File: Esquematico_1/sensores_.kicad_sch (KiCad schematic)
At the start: 12 parts, among them U1 ICM-42688-P, U3 Mag, U4 BMP388

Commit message: Footprints
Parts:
- R1, R2: footprint (none) -> Resistor_SMD:R_0805_2012Metric_Pad1.20x1.40mm_HandSolder
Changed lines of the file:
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@@
 			)
 		)
-		(property "Footprint" ""
+		(property "Footprint" "Resistor_SMD:R_0805_2012Metric_Pad1.20x1.40mm_HandSolder"
 			(at 27.432 78.74 90)
 			(effects
@@
 			)
 		)
-		(property "Footprint" ""
+		(property "Footprint" "Resistor_SMD:R_0805_2012Metric_Pad1.20x1.40mm_HandSolder"
 			(at 52.832 78.74 90)
 			(effects

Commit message: LDS y gran corrección de errores del esquemático
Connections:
- net GND: now also C1.2, U4.8 (VSS__1), U4.9 (VSS__2)
- no-connect marks 3 -> 13
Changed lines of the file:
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@@
 	(text_box "Especificaciones:\nSCK:\nSDA:\nVDD:\nGND:\nC1:\nGND:\nNC:\n"
 		(exclude_from_sim no)
-		(at 13.97 114.3 0)
-		(size 66.04 30.48)
+		(at 13.97 113.03 0)
+		(size 66.04 20.32)
 		(margins 0.9525 0.9525 0.9525 0.9525)
 		(stroke
@@
 	)
 	(junction
-		(at 158.75 104.14)
-		(diameter 0)
-		(color 0 0 0 0)
-	)
-	(junction
 		(at 86.36 49.53)
 		(diameter 0)
@@
 	)
 	(junction
+		(at 154.94 104.14)
+		(diameter 0)
+		(color 0 0 0 0)
+	)
+	(junction
 		(at 110.49 26.67)
 		(diameter 0)
@@
 	)
 	(junction
+		(at 143.51 104.14)
+		(diameter 0)
+		(color 0 0 0 0)
+	)
+	(junction
 		(at 99.06 29.21)
 		(diameter 0)
@@
 	)
 	(junction
-		(at 154.94 101.6)
+		(at 154.94 107.95)
 		(diameter 0)
 		(color 0 0 0 0)
@@
 	)
 	(no_connect
+		(at 35.56 93.98)
+	)
+	(no_connect
 		(at 83.82 39.37)
 	)
 	(no_connect
+		(at 35.56 101.6)
+	)
+	(no_connect
+		(at 35.56 88.9)
+	)
+	(no_connect
 		(at 83.82 44.45)
 	)
 	(no_connect
+		(at 53.34 93.98)
+	)
+	(no_connect
+		(at 53.34 88.9)
+	)
+	(no_connect
+		(at 35.56 91.44)
+	)
+	(no_connect
 		(at 83.82 41.91)
 	)
+	(no_connect
+		(at 53.34 86.36)
+	)
+	(no_connect
+		(at 35.56 99.06)
+	)
+	(no_connect
+		(at 53.34 91.44)
+	)
+	(no_connect
+		(at 35.56 96.52)
+	)
 	(wire
 		(pts
@@
 	(wire
 		(pts
+			(xy 140.97 106.68) (xy 143.51 106.68)
+		)
+		(stroke
+			(width 0)
+			(type default)
+		)
+	)
+	(wire
+		(pts
+			(xy 158.75 107.95) (xy 154.94 107.95)
+		)
+		(stroke
+			(width 0)
+			(type default)
+		)
+	)
+	(wire
+		(pts
 			(xy 26.67 83.82) (xy 29.21 83.82)
 		)
@@
 	(wire
 		(pts
+			(xy 143.51 101.6) (xy 143.51 104.14)
+		)
+		(stroke
+			(width 0)
+			(type default)
+		)
+	)
+	(wire
+		(pts
 			(xy 140.97 78.74) (xy 158.75 78.74)
 		)
@@
 	(wire
 		(pts
-			(xy 154.94 96.52) (xy 154.94 101.6)
-		)
-		(stroke
-			(width 0)
-			(type default)
-		)
-	)
-	(wire
-		(pts
 			(xy 154.94 74.93) (xy 158.75 74.93)
 		)
@@
 	(wire
 		(pts
+			(xy 154.94 104.14) (xy 154.94 107.95)
+		)
+		(stroke
+			(width 0)
+			(type default)
+		)
+	)
+	(wire
+		(pts
 			(xy 110.49 26.67) (xy 121.92 26.67)
 		)
@@
 	(wire
 		(pts
+			(xy 143.51 104.14) (xy 154.94 104.14)
+		)
+		(stroke
+			(width 0)
+			(type default)
+		)
+	)
+	(wire
+		(pts
 			(xy 27.94 39.37) (xy 33.02 39.37)
 		)
@@
 	(wire
 		(pts
+			(xy 143.51 106.68) (xy 143.51 104.14)
+		)
+		(stroke
+			(width 0)
+			(type default)
+		)
+	)
+	(wire
+		(pts
 			(xy 83.82 34.29) (xy 85.09 34.29)
 		)
@@
 	(wire
 		(pts
-			(xy 140.97 106.68) (xy 158.75 106.68)
-		)
-		(stroke
-			(width 0)
-			(type default)
-		)
-	)
-	(wire
-		(pts
 			(xy 53.34 96.52) (xy 57.15 96.52)
 		)
@@
 	(wire
 		(pts
-			(xy 140.97 101.6) (xy 154.94 101.6)
-		)
-		(stroke
-			(width 0)
-			(type default)
-		)
-	)
-	(wire
-		(pts
 			(xy 29.21 82.55) (xy 29.21 83.82)
 		)
@@
 	(wire
 		(pts
+			(xy 154.94 107.95) (xy 154.94 109.22)
+		)
+		(stroke
+			(width 0)
+			(type default)
+		)
+	)
+	(wire
+		(pts
 			(xy 27.94 44.45) (xy 33.02 44.45)
 		)
@@
 	(wire
 		(pts
-			(xy 158.75 104.14) (xy 158.75 90.17)
+			(xy 158.75 90.17) (xy 158.75 107.95)
 		)
 		(stroke
@@
 	(wire
 		(pts
+			(xy 140.97 101.6) (xy 143.51 101.6)
+		)
+		(stroke
+			(width 0)
+			(type default)
+		)
+	)
+	(wire
+		(pts
 			(xy 121.92 26.67) (xy 121.92 25.4)
 		)
@@
 	(wire
 		(pts
-			(xy 140.97 104.14) (xy 158.75 104.14)
-		)
-		(stroke
-			(width 0)
-			(type default)
-		)
-	)
-	(wire
-		(pts
-			(xy 158.75 106.68) (xy 158.75 104.14)
-		)
-		(stroke
-			(width 0)
-			(type default)
-		)
-	)
-	(wire
-		(pts
 			(xy 58.42 99.06) (xy 58.42 96.52)
 		)
@@
 	(wire
 		(pts
+			(xy 140.97 104.14) (xy 143.51 104.14)
+		)
+		(stroke
+			(width 0)
+			(type default)
+		)
+	)
+	(wire
+		(pts
 			(xy 54.61 72.39) (xy 29.21 72.39)
 		)
@@
 	(wire
 		(pts
-			(xy 154.94 101.6) (xy 154.94 109.22)
-		)
-		(stroke
+			(xy 154.94 96.52) (xy 154.94 104.14)
+		)
+		(stroke

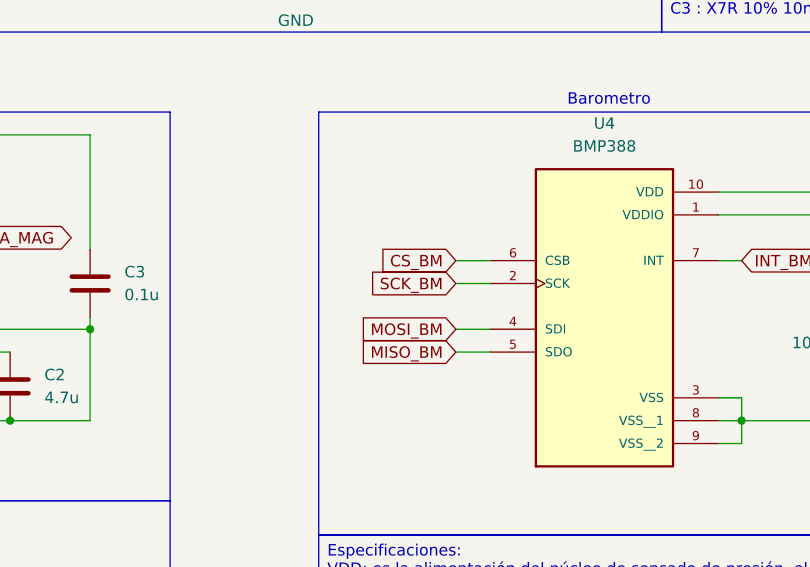
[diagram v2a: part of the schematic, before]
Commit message: Cambios netclasses, rules en el PCB, conección de los cristales
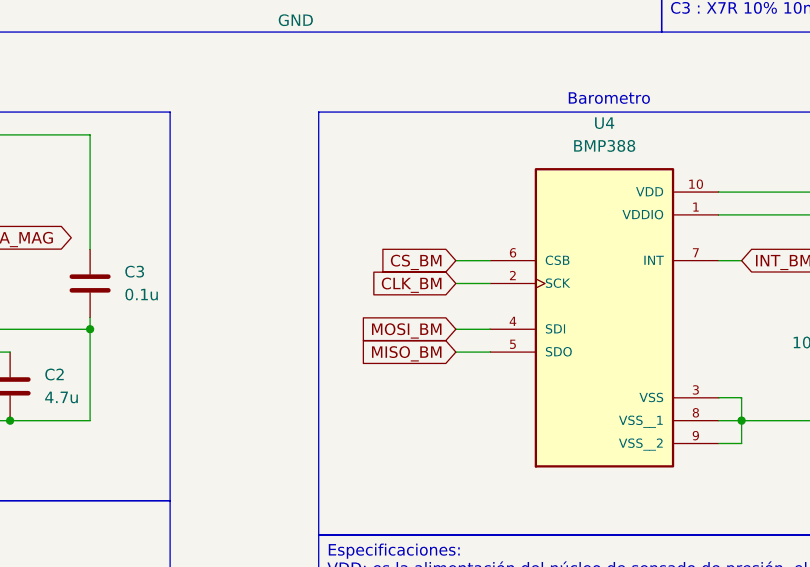
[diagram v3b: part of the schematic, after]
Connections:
- net SCK_BM renamed CLK_BM
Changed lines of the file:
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@@
 		)
 	)
-	(global_label "SCK_BM"
+	(global_label "CLK_BM"
 		(shape input)
 		(at 111.76 88.9 180)
@@
 		)
 		(property "Intersheetrefs" "${INTERSHEET_REFS}"
-			(at 101.3363 88.9 0)
+			(at 101.5177 88.9 0)
 			(effects
 				(font

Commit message: Cristal corregido
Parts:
- C1, C4: footprint Capacitor_SMD:C_0805_2012Metric_Pad1.18x1.45mm_HandSolder -> Capacitor_SMD:C_0603_1608Metric_Pad1.08x0.95mm_HandSolder
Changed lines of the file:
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@@
 			)
 		)
-		(property "Footprint" "Capacitor_SMD:C_0805_2012Metric_Pad1.18x1.45mm_HandSolder"
+		(property "Footprint" "Capacitor_SMD:C_0603_1608Metric_Pad1.08x0.95mm_HandSolder"
 			(at 159.7152 90.17 0)
 			(effects
@@
 			)
 		)
-		(property "Footprint" "Capacitor_SMD:C_0805_2012Metric_Pad1.18x1.45mm_HandSolder"
+		(property "Footprint" "Capacitor_SMD:C_0603_1608Metric_Pad1.08x0.95mm_HandSolder"
 			(at 155.9052 96.52 0)
 			(effects

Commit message: Cambio de la SD, re ruteo del ESC para mayor fiabilidad, correción en el clearence
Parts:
- C11, C9: footprint Capacitor_SMD:C_0805_2012Metric_Pad1.18x1.45mm_HandSolder -> Capacitor_SMD:C_0603_1608Metric_Pad1.08x0.95mm_HandSolder
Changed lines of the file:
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@@
 			)
 		)
-		(property "Footprint" "Capacitor_SMD:C_0805_2012Metric_Pad1.18x1.45mm_HandSolder"
+		(property "Footprint" "Capacitor_SMD:C_0603_1608Metric_Pad1.08x0.95mm_HandSolder"
 			(at 111.4552 36.83 0)
 			(effects
@@
 			)
 		)
-		(property "Footprint" "Capacitor_SMD:C_0805_2012Metric_Pad1.18x1.45mm_HandSolder"
+		(property "Footprint" "Capacitor_SMD:C_0603_1608Metric_Pad1.08x0.95mm_HandSolder"
 			(at 100.0252 38.1 0)
 			(effects

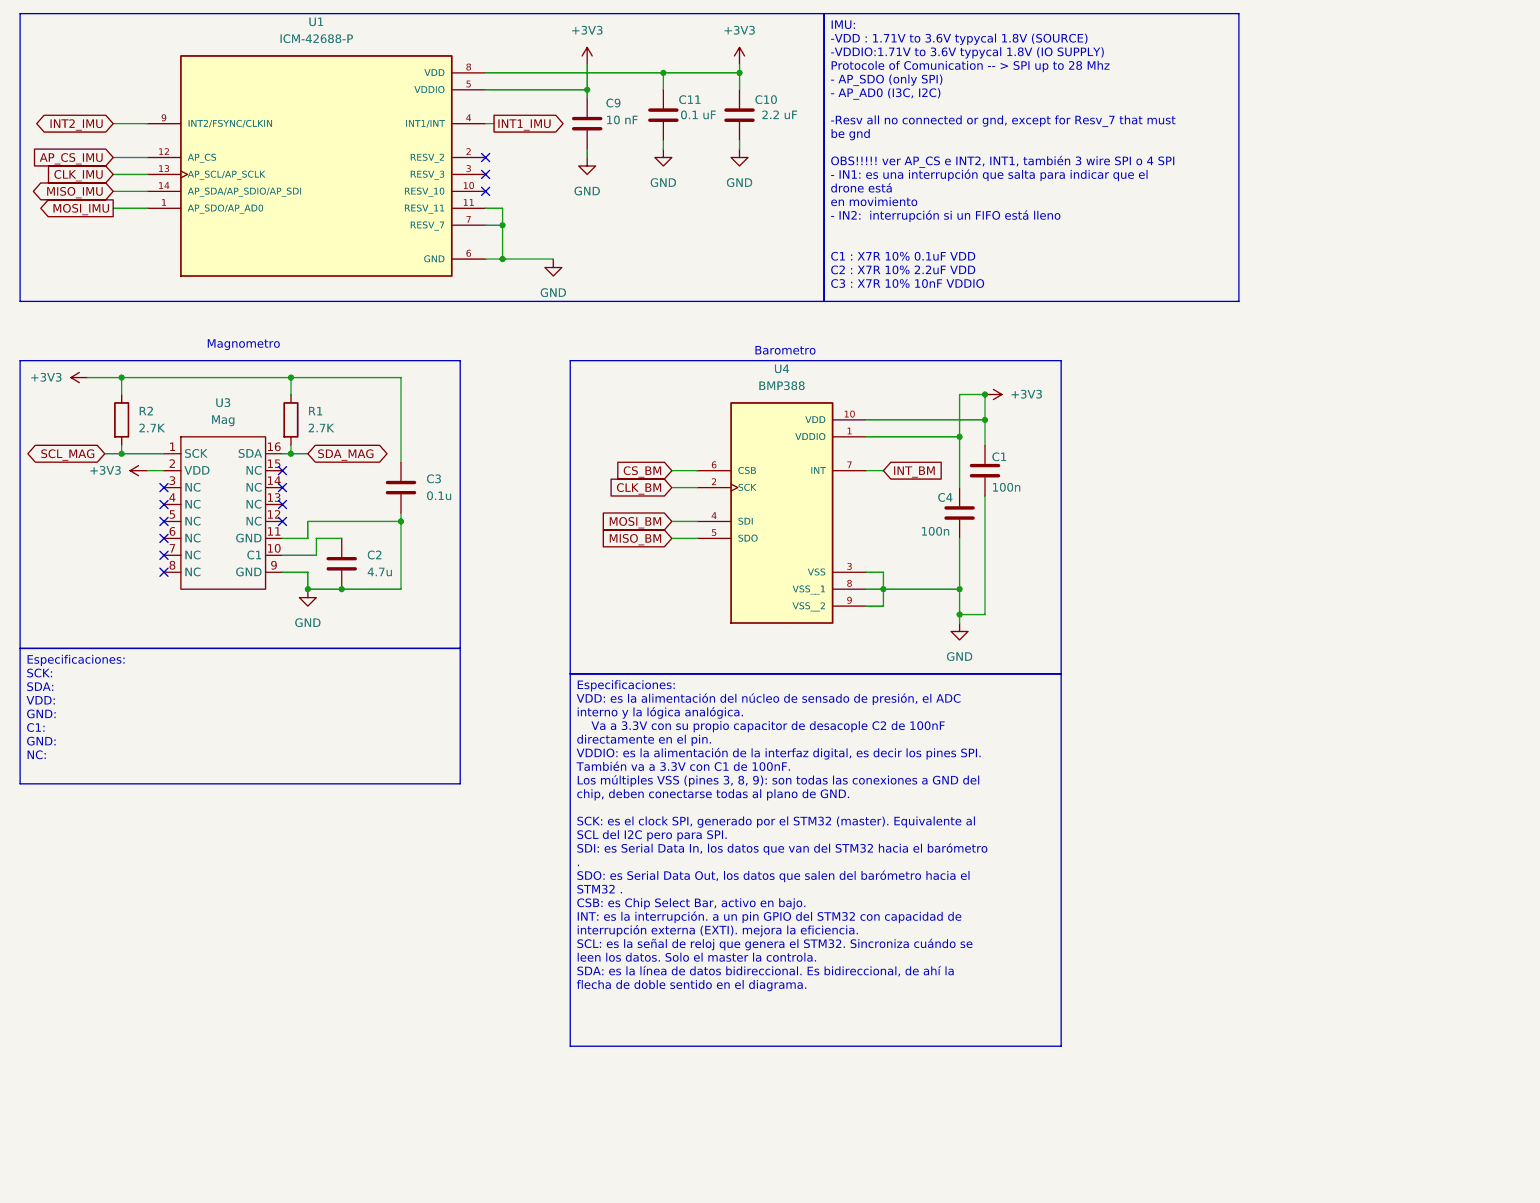
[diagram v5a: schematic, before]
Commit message: Cambio de magnometro :c
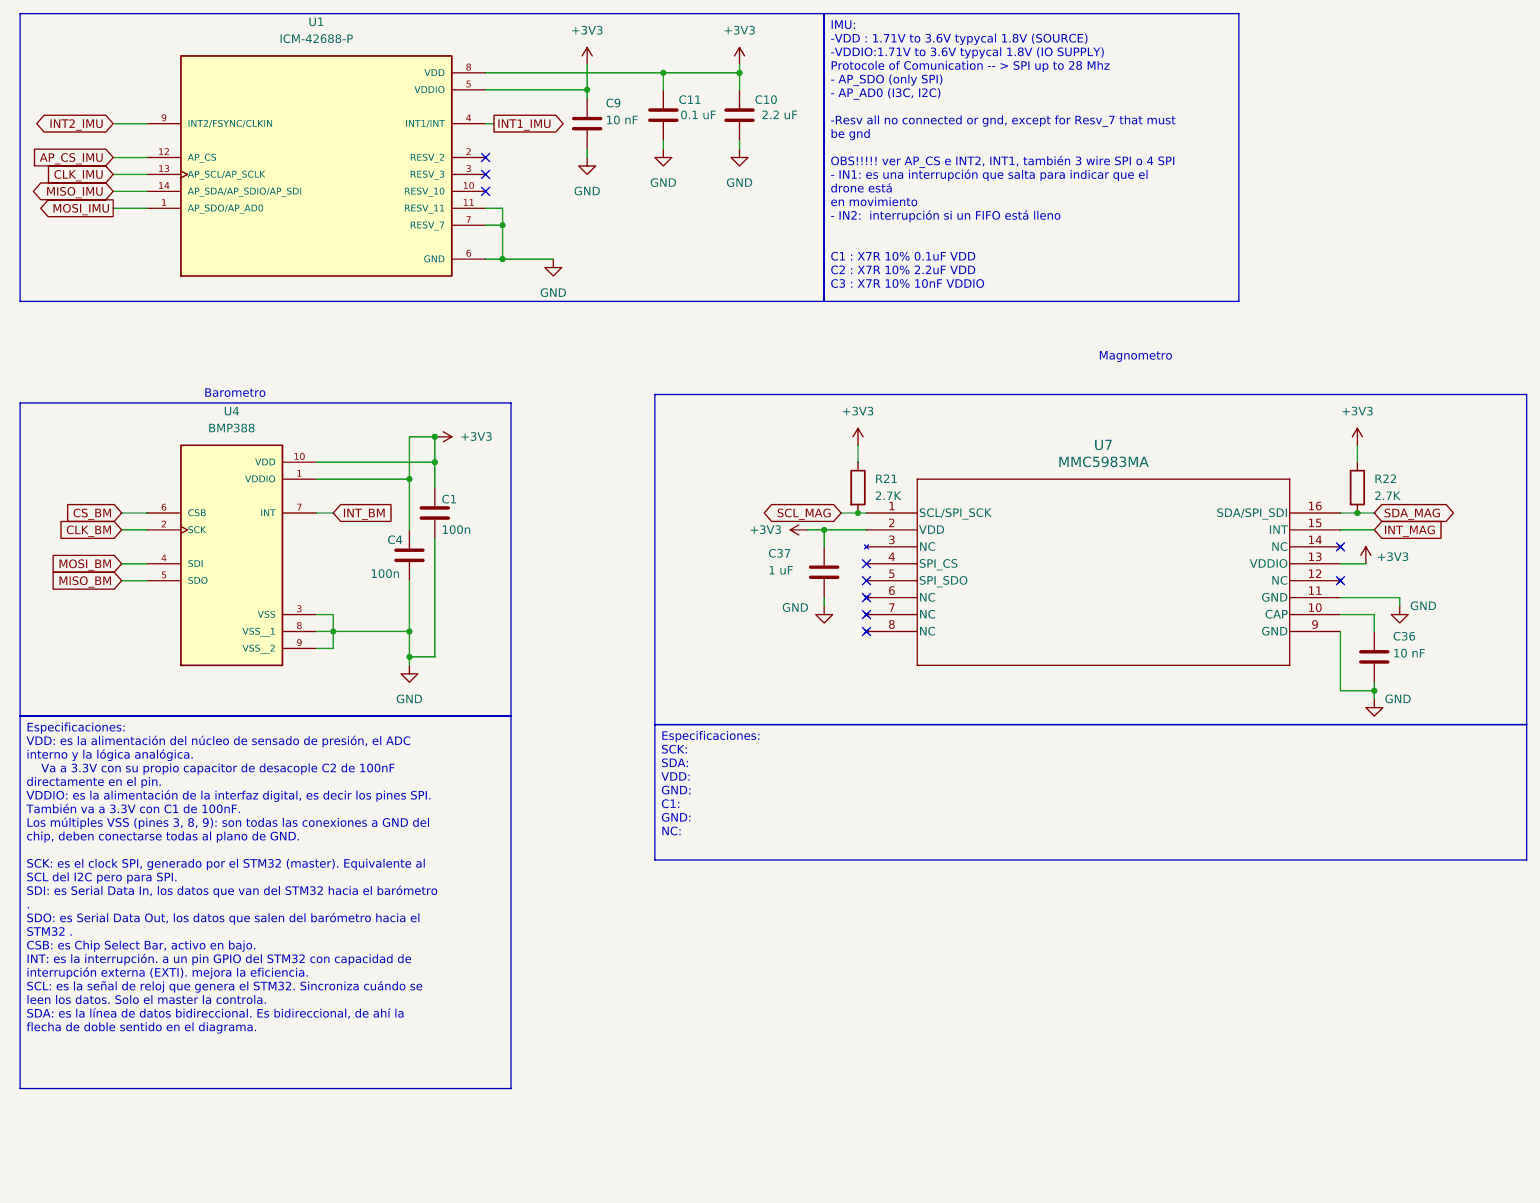
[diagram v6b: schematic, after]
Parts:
- removed C2: 4.7u, Capacitor_SMD:C_0805_2012Metric_Pad1.18x1.45mm_HandSolder, symbol Device:C
- removed C3: 0.1u, Capacitor_SMD:C_0805_2012Metric_Pad1.18x1.45mm_HandSolder, symbol Device:C
- removed R1, R2: 2.7K, Resistor_SMD:R_0805_2012Metric_Pad1.20x1.40mm_HandSolder, symbol Device:R
- removed U3: Mag, QMC588P:LGA-16_L3.0-W3.0-P0.50-BL_SQ, symbol qmc5883p:QMC5883P
- added C36: 10 nF, Capacitor_SMD:C_0603_1608Metric_Pad1.08x0.95mm_HandSolder, symbol Device:C
- added C37: 1 uF, Capacitor_SMD:C_0603_1608Metric_Pad1.08x0.95mm_HandSolder, symbol Device:C
- added R21, R22: 2.7K, Resistor_SMD:R_0805_2012Metric_Pad1.20x1.40mm_HandSolder, symbol Device:R
- added U7: MMC5983MA, MMC5983MA:MMC5983MA_MEM, symbol MMC5983MA:MMC5983MA
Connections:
- net +3V3: now also C37.1, R21.1, R22.1, U7.13 (VDDIO), U7.2 (VDD)
- net GND: now also C36.2, C37.2, U7.11 (GND), U7.9 (GND)
- net SCL_MAG: now also R21.2, U7.1 (SCL/SPI_SCK)
- net SDA_MAG: now also R22.2, U7.16 (SDA/SPI_SDI)
- new net: C36.1, U7.10 (CAP)
- new net INT_MAG: U7.15 (INT)
- no-connect marks 13 -> 10
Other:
- moved on the sheet: C1, C4, U4

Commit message: Cambio de IMU, creación del BOM
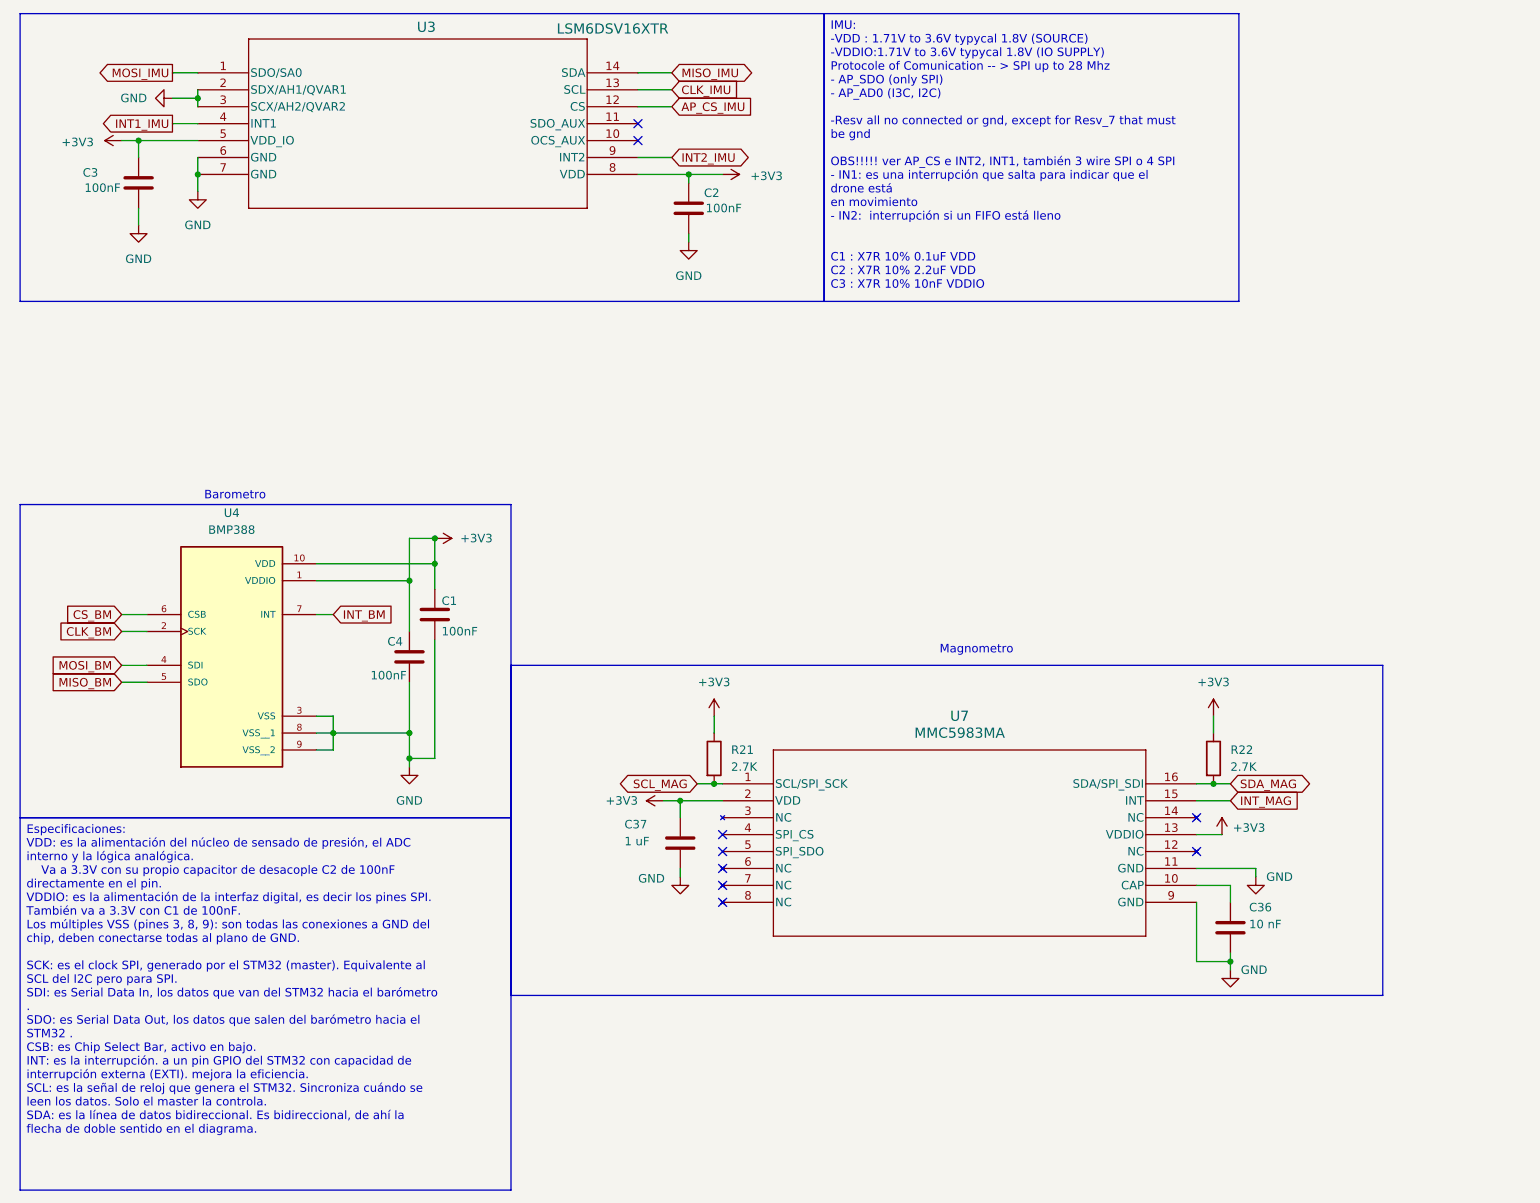
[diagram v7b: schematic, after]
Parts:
- removed C10: 2.2 uF, Capacitor_SMD:C_0805_2012Metric_Pad1.18x1.45mm_HandSolder, symbol Device:C
- removed C11: 0.1 uF, Capacitor_SMD:C_0603_1608Metric_Pad1.08x0.95mm_HandSolder, symbol Device:C
- removed C9: 10 nF, Capacitor_SMD:C_0603_1608Metric_Pad1.08x0.95mm_HandSolder, symbol Device:C
- removed U1: ICM-42688-P, ICM_42688_P:PQFN50P300X250X97-14N, symbol ICM-42688-P:ICM-42688-P
- added C2, C3: 100nF, Capacitor_SMD:C_0603_1608Metric_Pad1.08x0.95mm_HandSolder, symbol Device:C
- added U3: LSM6DSV16XTR, LSM6DSV16XTR:LGA-14L_STM, symbol LSM6DSV16XTR:LSM6DSV16XTR
- C1, C4: value 100n -> 100nF; LCSC Part Name (none) -> C1591
- C36: LCSC Part Name (none) -> C1589
- C37: LCSC Part Name (none) -> C29936
- R21, R22: now left out of the parts list
- U4: LCSC Part Name (none) -> C779278
- U7: LCSC Part Name (none) -> C404329
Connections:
- net +3V3: now also C2.1, C3.1, U3.5 (VDD_IO), U3.8 (VDD)
- net AP_CS_IMU: now also U3.12 (CS)
- net CLK_IMU: now also U3.13 (SCL)
- net GND: now also C2.2, C3.2, U3.2 (SDX/AH1/QVAR1), U3.3 (SCX/AH2/QVAR2), U3.6 (GND), U3.7 (GND)
- net INT1_IMU: now also U3.4 (INT1)
- net INT2_IMU: now also U3.9 (INT2)
- net MISO_IMU: now also U3.14 (SDA)
- net MOSI_IMU: now also U3.1 (SDO/SA0)
- no-connect marks 10 -> 9
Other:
- moved on the sheet: C1, C36, C37, C4, R21, R22, U4, U7
